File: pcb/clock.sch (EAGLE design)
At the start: 0 parts

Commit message: Started PCB
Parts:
- added C1: 0.1uF, rcl:C-US025-025X050
- added C2, C3: 10uF, rcl:C-US025-025X050
- added C4: 1000uF, rcl:CPOL-USE3.5-8
- added CN1: (no value), adafruit:DCBARRELPTH
- added JP1: FTDI, pinhead:PINHD-1X6/90
- added JP2: (no value), pinhead:PINHD-1X2
- added JP3: 74AHCT125, ic-package:DIL14
- added R1, R3, R4, R5: 470, rcl:R-US_0207/10
- added R2: 10K, rcl:R-US_0207/10
- added U1: ESP-01, diy-modules:WIRELESS-WIFI-ESP-01
- added U2: LD1117V33, my-custom:LD1117
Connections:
- new net +5V: C1.1, C4.+, CN1.PWR, JP1.3, JP3.14, U2.VIN
- new net DTR: JP1.6
- new net GND: C1.2, C2.2, C3.2, C4.-, CN1.GND, JP1.1, JP1.2, JP2.2, JP3.1, JP3.4, JP3.7, R5.1, U1.GND
- new net GPIO2: JP3.2, U1.GPIO2
- new net N$1: JP2.1, R1.2
- new net N$2: R2.1, U1.CH_PD, U1.RST
- new net N$3: R4.1, R5.2
- new net NP_DATA: JP3.3, R1.1
- new net RXD_3V3: R3.1, R4.2, U1.URXD
- new net RXD_5V: JP1.5, R3.2
- new net TXD_3V3: JP3.5, U1.UTXD
- new net TXD_5V: JP1.4, JP3.6
- new net VCC: C2.1, C3.1, R2.2, U1.VCC, U2.VOUT

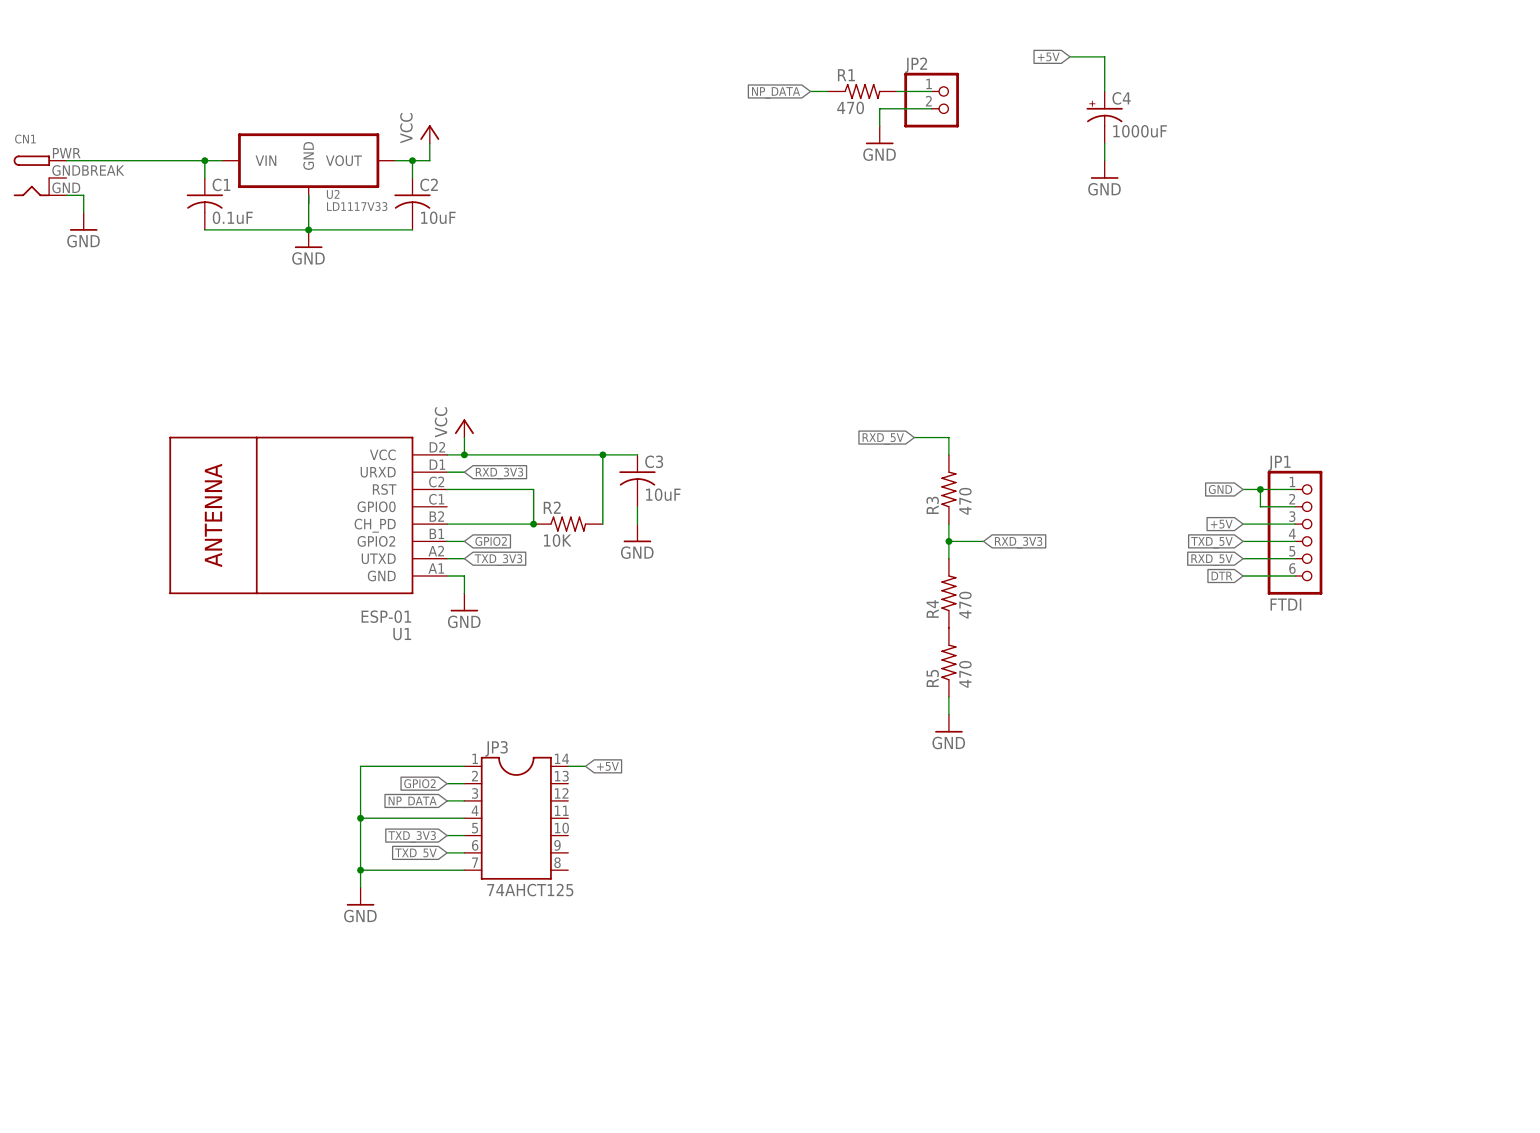
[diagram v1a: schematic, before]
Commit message: Added button
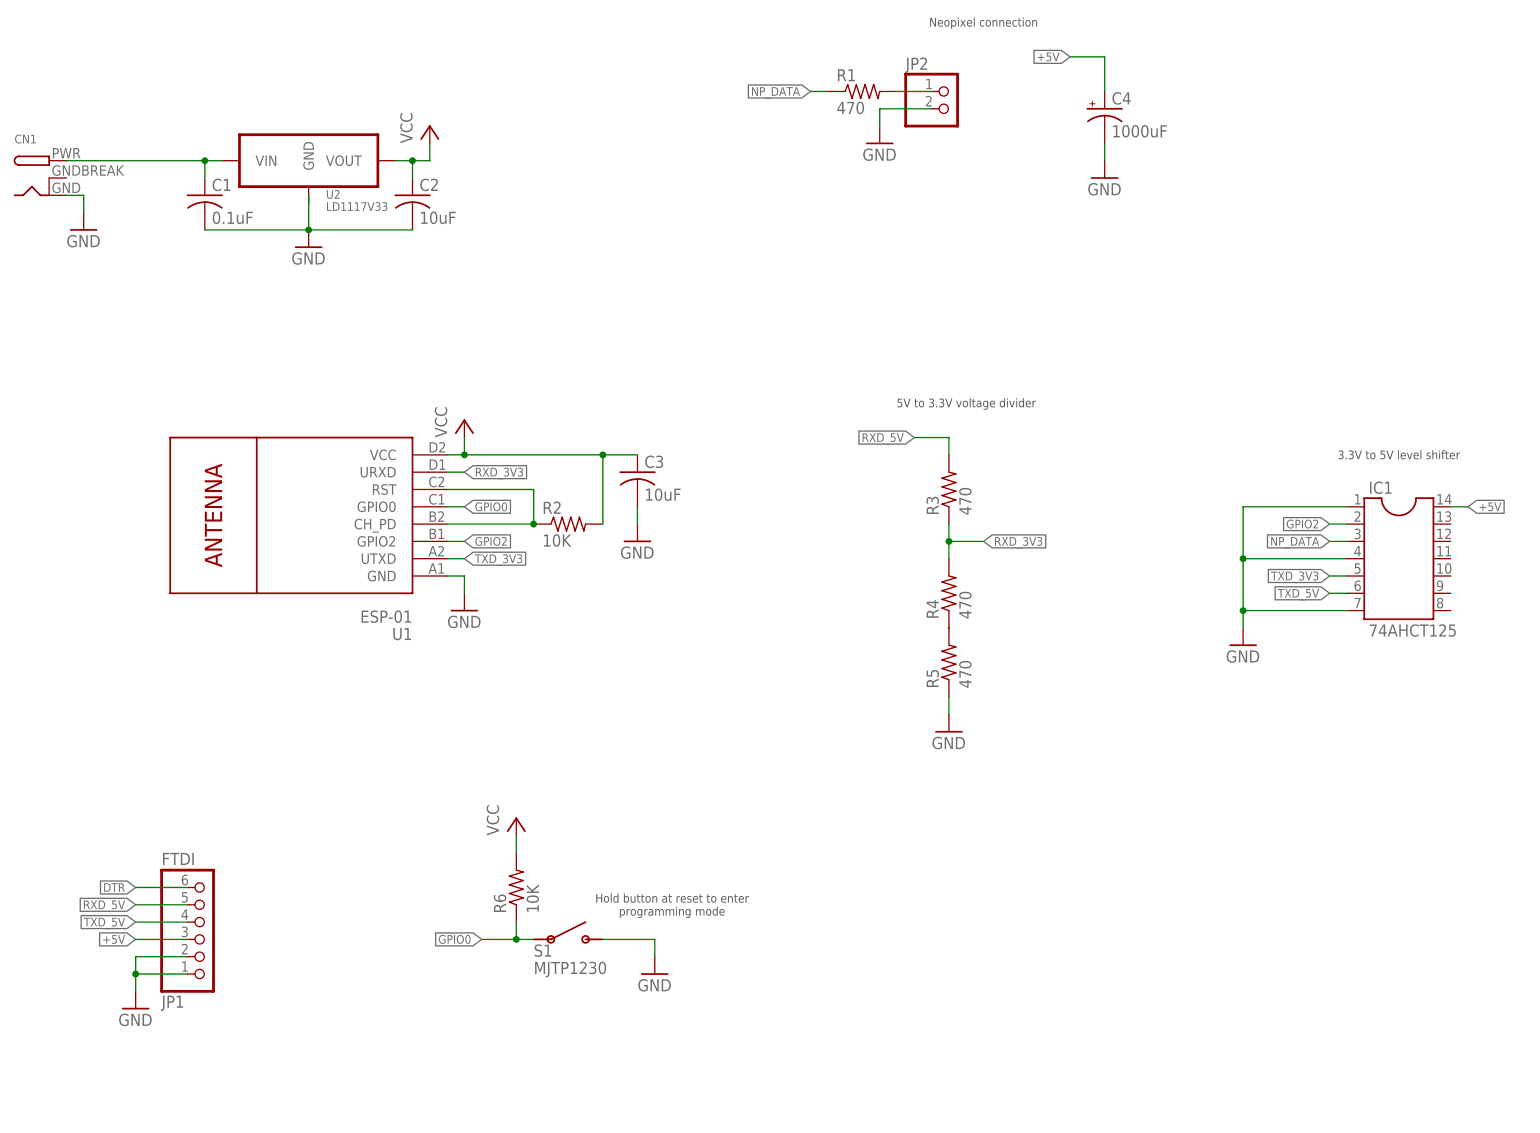
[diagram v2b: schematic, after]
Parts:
- removed JP3: 74AHCT125, ic-package:DIL14
- added IC1: 74AHCT125, ic-package:DIL14
- added R6: 10K, rcl:R-US_0207/10
- added S1: MJTP1230, my-custom:TACTILE-BUTTON-MJTP1230
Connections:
- new net GPIO0: R6.1, S1.1, U1.GPIO0
- net +5V: now also IC1.14; no longer JP3.14
- net GND: now also IC1.1, IC1.4, IC1.7, S1.3; no longer JP3.1, JP3.4, JP3.7
- net GPIO2: now also IC1.2; no longer JP3.2
- net NP_DATA: now also IC1.3; no longer JP3.3
- net TXD_3V3: now also IC1.5; no longer JP3.5
- net TXD_5V: now also IC1.6; no longer JP3.6
- net VCC: now also R6.2
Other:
- note added: "3.3V to 5V level shifter"
- note added: "5V to 3.3V voltage divider"
- note added: "Hold button at reset to enter programming mode"
- note added: "Neopixel connection"
- moved on the sheet: JP1
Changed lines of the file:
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@@
 <part name="R5" library="rcl" deviceset="R-US_" device="0207/10" value="470"/>
 <part name="GND7" library="supply1" deviceset="GND" device=""/>
-<part name="JP3" library="ic-package" deviceset="DIL14" device="" value="74AHCT125"/>
+<part name="IC1" library="ic-package" deviceset="DIL14" device="" value="74AHCT125"/>
 <part name="GND8" library="supply1" deviceset="GND" device=""/>
+<part name="S1" library="my-custom" deviceset="TACTILE-BUTTON-MJTP1230" device="" value="MJTP1230"/>
+<part name="GND9" library="supply1" deviceset="GND" device=""/>
+<part name="GND10" library="supply1" deviceset="GND" device=""/>
+<part name="P+3" library="supply1" deviceset="VCC" device=""/>
+<part name="R6" library="rcl" deviceset="R-US_" device="0207/10" value="10K"/>
 </parts>
 <sheets>
 <sheet>
 <plain>
+<text x="114.3" y="40.64" size="1.27" layer="97" align="center">Hold button at reset to enter
+programming mode</text>
+<text x="157.48" y="114.3" size="1.27" layer="97" align="center">5V to 3.3V voltage divider</text>
+<text x="220.98" y="106.68" size="1.27" layer="97" align="center">3.3V to 5V level shifter</text>
+<text x="160.02" y="170.18" size="1.27" layer="97" align="center">Neopixel connection</text>
 </plain>
 <instances>
@@
 <instance part="C1" gate="G$1" x="45.72" y="144.78"/>
 <instance part="C2" gate="G$1" x="76.2" y="144.78"/>
-<instance part="JP1" gate="A" x="208.28" y="93.98"/>
+<instance part="JP1" gate="A" x="45.72" y="38.1" rot="MR180"/>
 <instance part="C3" gate="G$1" x="109.22" y="104.14"/>
 <instance part="GND3" gate="1" x="109.22" y="93.98"/>
@@
 <instance part="R5" gate="G$1" x="154.94" y="76.2" rot="R90"/>
 <instance part="GND7" gate="1" x="154.94" y="66.04"/>
-<instance part="JP3" gate="G$1" x="91.44" y="53.34"/>
-<instance part="GND8" gate="1" x="68.58" y="40.64"/>
+<instance part="IC1" gate="G$1" x="220.98" y="91.44"/>
+<instance part="GND8" gate="1" x="198.12" y="78.74"/>
+<instance part="S1" gate="G$1" x="99.06" y="35.56"/>
+<instance part="GND9" gate="1" x="35.56" y="25.4"/>
+<instance part="GND10" gate="1" x="111.76" y="30.48"/>
+<instance part="P+3" gate="VCC" x="91.44" y="53.34"/>
+<instance part="R6" gate="G$1" x="91.44" y="43.18" rot="R90"/>
 </instances>
 <busses>
@@
 <segment>
 <pinref part="JP1" gate="A" pin="3"/>
-<wire x1="205.74" y1="96.52" x2="198.12" y2="96.52" width="0.1524" layer="91"/>
-<label x="198.12" y="96.52" size="1.27" layer="95" rot="R180" xref="yes"/>
+<wire x1="43.18" y1="35.56" x2="35.56" y2="35.56" width="0.1524" layer="91"/>
+<label x="35.56" y="35.56" size="1.27" layer="95" rot="MR0" xref="yes"/>
 </segment>
 <segment>
@@
 </segment>
 <segment>
-<label x="101.6" y="60.96" size="1.27" layer="95" xref="yes"/>
-<pinref part="JP3" gate="G$1" pin="14"/>
-<wire x1="99.06" y1="60.96" x2="101.6" y2="60.96" width="0.1524" layer="91"/>
+<label x="231.14" y="99.06" size="1.27" layer="95" xref="yes"/>
+<pinref part="IC1" gate="G$1" pin="14"/>
+<wire x1="228.6" y1="99.06" x2="231.14" y2="99.06" width="0.1524" layer="91"/>
 </segment>
 </net>
@@
 <junction x="104.14" y="106.68"/>
 </segment>
+<segment>
+<pinref part="P+3" gate="VCC" pin="VCC"/>
+<pinref part="R6" gate="G$1" pin="2"/>
+<wire x1="91.44" y1="50.8" x2="91.44" y2="48.26" width="0.1524" layer="91"/>
+</segment>
 </net>
 <net name="GND" class="0">
@@
 <segment>
 <pinref part="JP1" gate="A" pin="1"/>
-<wire x1="205.74" y1="101.6" x2="200.66" y2="101.6" width="0.1524" layer="91"/>
-<label x="198.12" y="101.6" size="1.27" layer="95" rot="R180" xref="yes"/>
+<wire x1="43.18" y1="30.48" x2="35.56" y2="30.48" width="0.1524" layer="91"/>
+<wire x1="35.56" y1="30.48" x2="35.56" y2="27.94" width="0.1524" layer="91"/>
+<pinref part="GND9" gate="1" pin="GND"/>
 <pinref part="JP1" gate="A" pin="2"/>
-<wire x1="200.66" y1="101.6" x2="198.12" y2="101.6" width="0.1524" layer="91"/>
-<wire x1="205.74" y1="99.06" x2="200.66" y2="99.06" width="0.1524" layer="91"/>
-<wire x1="200.66" y1="99.06" x2="200.66" y2="101.6" width="0.1524" layer="91"/>
-<junction x="200.66" y="101.6"/>
+<wire x1="43.18" y1="33.02" x2="35.56" y2="33.02" width="0.1524" layer="91"/>
+<wire x1="35.56" y1="33.02" x2="35.56" y2="30.48" width="0.1524" layer="91"/>
+<junction x="35.56" y="30.48"/>
 </segment>
 <segment>
@@
 </segment>
 <segment>
-<pinref part="JP3" gate="G$1" pin="1"/>
+<pinref part="IC1" gate="G$1" pin="1"/>
 <pinref part="GND8" gate="1" pin="GND"/>
-<wire x1="83.82" y1="60.96" x2="68.58" y2="60.96" width="0.1524" layer="91"/>
-<wire x1="68.58" y1="60.96" x2="68.58" y2="53.34" width="0.1524" layer="91"/>
-<wire x1="68.58" y1="53.34" x2="68.58" y2="45.72" width="0.1524" layer="91"/>
-<wire x1="68.58" y1="45.72" x2="68.58" y2="43.18" width="0.1524" layer="91"/>
-<junction x="68.58" y="45.72"/>
-<pinref part="JP3" gate="G$1" pin="7"/>
-<wire x1="68.58" y1="45.72" x2="83.82" y2="45.72" width="0.1524" layer="91"/>
-<pinref part="JP3" gate="G$1" pin="4"/>
-<wire x1="83.82" y1="53.34" x2="68.58" y2="53.34" width="0.1524" layer="91"/>
-<junction x="68.58" y="53.34"/>
+<wire x1="213.36" y1="99.06" x2="198.12" y2="99.06" width="0.1524" layer="91"/>
+<wire x1="198.12" y1="99.06" x2="198.12" y2="91.44" width="0.1524" layer="91"/>
+<wire x1="198.12" y1="91.44" x2="198.12" y2="83.82" width="0.1524" layer="91"/>
+<wire x1="198.12" y1="83.82" x2="198.12" y2="81.28" width="0.1524" layer="91"/>
+<junction x="198.12" y="83.82"/>
+<pinref part="IC1" gate="G$1" pin="7"/>
+<wire x1="198.12" y1="83.82" x2="213.36" y2="83.82" width="0.1524" layer="91"/>
+<pinref part="IC1" gate="G$1" pin="4"/>
+<wire x1="213.36" y1="91.44" x2="198.12" y2="91.44" width="0.1524" layer="91"/>
+<junction x="198.12" y="91.44"/>
+</segment>
+<segment>
+<pinref part="S1" gate="G$1" pin="3"/>
+<wire x1="104.14" y1="35.56" x2="111.76" y2="35.56" width="0.1524" layer="91"/>
+<wire x1="111.76" y1="35.56" x2="111.76" y2="33.02" width="0.1524" layer="91"/>
+<pinref part="GND10" gate="1" pin="GND"/>
 </segment>
 </net>
@@
 <segment>
 <pinref part="JP1" gate="A" pin="4"/>
-<wire x1="205.74" y1="93.98" x2="198.12" y2="93.98" width="0.1524" layer="91"/>
-<label x="198.12" y="93.98" size="1.27" layer="95" rot="R180" xref="yes"/>
-</segment>
-<segment>
-<label x="81.28" y="48.26" size="1.27" layer="95" rot="R180" xref="yes"/>
-<pinref part="JP3" gate="G$1" pin="6"/>
-<wire x1="81.28" y1="48.26" x2="83.82" y2="48.26" width="0.1524" layer="91"/>
+<wire x1="43.18" y1="38.1" x2="35.56" y2="38.1" width="0.1524" layer="91"/>
+<label x="35.56" y="38.1" size="1.27" layer="95" rot="MR0" xref="yes"/>
+</segment>
+<segment>
+<label x="210.82" y="86.36" size="1.27" layer="95" rot="R180" xref="yes"/>
+<pinref part="IC1" gate="G$1" pin="6"/>
+<wire x1="210.82" y1="86.36" x2="213.36" y2="86.36" width="0.1524" layer="91"/>
 </segment>
 </net>
@@
 <segment>
 <pinref part="JP1" gate="A" pin="5"/>
-<wire x1="205.74" y1="91.44" x2="198.12" y2="91.44" width="0.1524" layer="91"/>
-<label x="198.12" y="91.44" size="1.27" layer="95" rot="R180" xref="yes"/>
+<wire x1="43.18" y1="40.64" x2="35.56" y2="40.64" width="0.1524" layer="91"/>
+<label x="35.56" y="40.64" size="1.27" layer="95" rot="MR0" xref="yes"/>
 </segment>
 <segment>
@@
 <segment>
 <pinref part="JP1" gate="A" pin="6"/>
-<wire x1="205.74" y1="88.9" x2="198.12" y2="88.9" width="0.1524" layer="91"/>
-<label x="198.12" y="88.9" size="1.27" layer="95" rot="R180" xref="yes"/>
+<wire x1="43.18" y1="43.18" x2="35.56" y2="43.18" width="0.1524" layer="91"/>
+<label x="35.56" y="43.18" size="1.27" layer="95" rot="MR0" xref="yes"/>
 </segment>
 </net>
@@
 </segment>
 <segment>
-<label x="81.28" y="50.8" size="1.27" layer="95" rot="R180" xref="yes"/>
-<pinref part="JP3" gate="G$1" pin="5"/>
-<wire x1="81.28" y1="50.8" x2="83.82" y2="50.8" width="0.1524" layer="91"/>
+<label x="210.82" y="88.9" size="1.27" layer="95" rot="R180" xref="yes"/>
+<pinref part="IC1" gate="G$1" pin="5"/>
+<wire x1="210.82" y1="88.9" x2="213.36" y2="88.9" width="0.1524" layer="91"/>
 </segment>
 </net>
@@
 </segment>
 <segment>
-<label x="81.28" y="55.88" size="1.27" layer="95" rot="R180" xref="yes"/>
-<pinref part="JP3" gate="G$1" pin="3"/>
-<wire x1="81.28" y1="55.88" x2="83.82" y2="55.88" width="0.1524" layer="91"/>
+<label x="210.82" y="93.98" size="1.27" layer="95" rot="R180" xref="yes"/>
+<pinref part="IC1" gate="G$1" pin="3"/>
+<wire x1="210.82" y1="93.98" x2="213.36" y2="93.98" width="0.1524" layer="91"/>
 </segment>
 </net>
@@
 <net name="GPIO2" class="0">
 <segment>
-<label x="81.28" y="58.42" size="1.27" layer="95" rot="R180" xref="yes"/>
-<pinref part="JP3" gate="G$1" pin="2"/>
-<wire x1="83.82" y1="58.42" x2="81.28" y2="58.42" width="0.1524" layer="91"/>
+<label x="210.82" y="96.52" size="1.27" layer="95" rot="R180" xref="yes"/>
+<pinref part="IC1" gate="G$1" pin="2"/>
+<wire x1="213.36" y1="96.52" x2="210.82" y2="96.52" width="0.1524" layer="91"/>
 </segment>
 <segment>
@@
 <wire x1="81.28" y1="93.98" x2="83.82" y2="93.98" width="0.1524" layer="91"/>
 <label x="83.82" y="93.98" size="1.27" layer="95" xref="yes"/>
+</segment>
+</net>
+<net name="GPIO0" class="0">
+<segment>
+<pinref part="U1" gate="G$1" pin="GPIO0"/>
+<wire x1="81.28" y1="99.06" x2="83.82" y2="99.06" width="0.1524" layer="91"/>
+<label x="83.82" y="99.06" size="1.27" layer="95" xref="yes"/>
+</segment>
+<segment>
+<pinref part="S1" gate="G$1" pin="1"/>
+<wire x1="93.98" y1="35.56" x2="91.44" y2="35.56" width="0.1524" layer="91"/>
+<wire x1="91.44" y1="35.56" x2="86.36" y2="35.56" width="0.1524" layer="91"/>
+<wire x1="91.44" y1="35.56" x2="91.44" y2="38.1" width="0.1524" layer="91"/>
+<junction x="91.44" y="35.56"/>
+<pinref part="R6" gate="G$1" pin="1"/>
+<label x="86.36" y="35.56" size="1.27" layer="95" rot="R180" xref="yes"/>
 </segment>
 </net>
@@
 </schematic>
 </drawing>
+<compatibility>
+<note version="6.3" minversion="6.2.2" severity="warning">
+Since Version 6.2.2 text objects can contain more than one line,
+which will not be processed correctly with this version.
+</note>
+</compatibility>
 </eagle>
